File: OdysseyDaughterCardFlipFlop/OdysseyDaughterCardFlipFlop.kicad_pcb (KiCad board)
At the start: 2 copper layers, 39.9 x 46.6 mm, 17 parts, among them J1 Conn_01x02, Q1 2N3906, Q2 2N3906, Q3 BC547C, Q4 BC547C, X1 OdysseyDaughterCard

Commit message: OdysseyDaughterCardFlipFlop: Open and close in Kicad 6, fix symbol library path
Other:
- net class Default removed

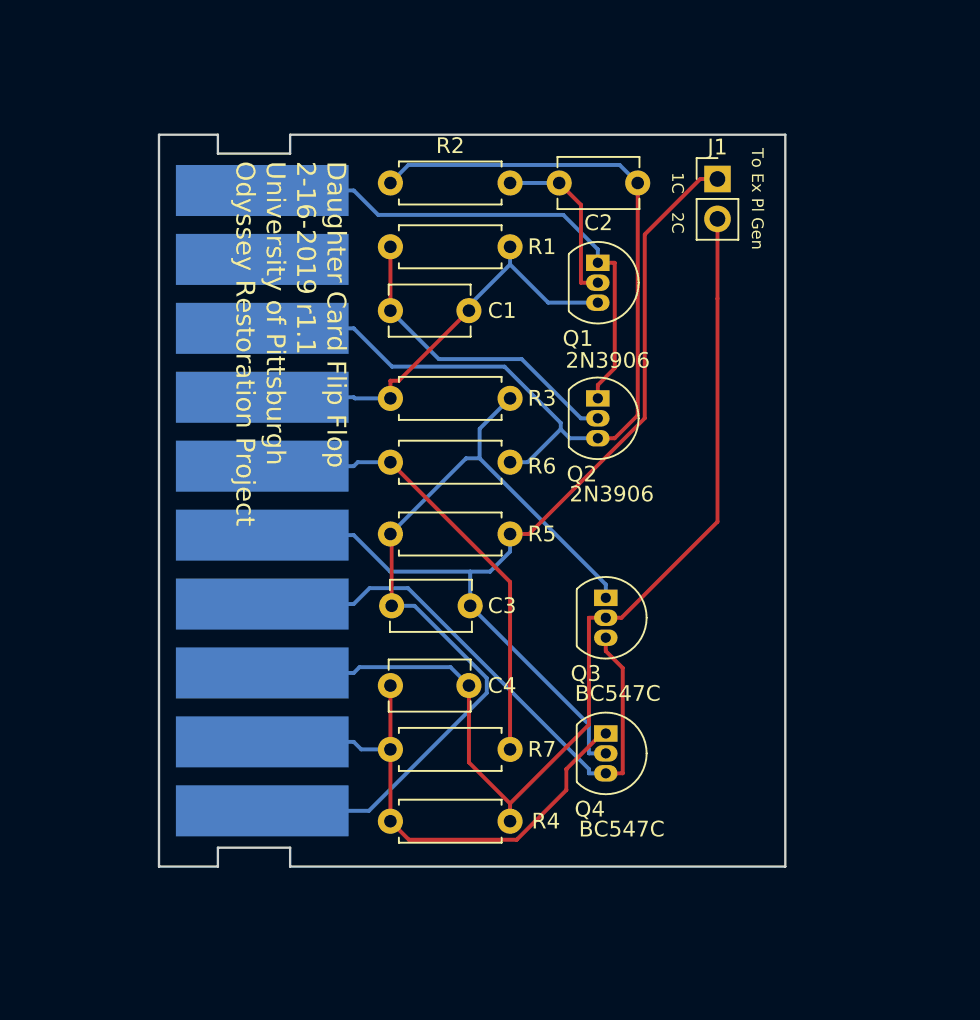
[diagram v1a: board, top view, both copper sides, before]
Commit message: OdysseyDaughterCardFlipFlop wider transistor footprint, logo, pours, pdfs, images, 3d model
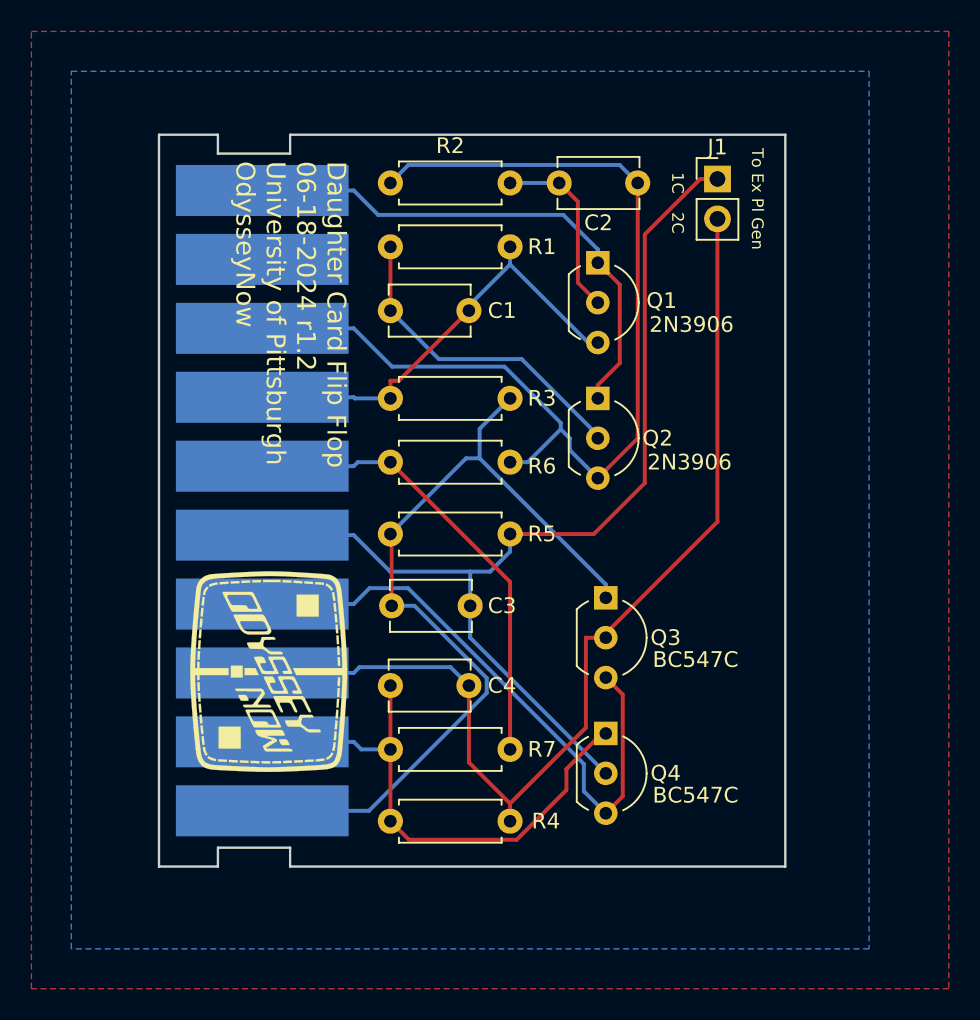
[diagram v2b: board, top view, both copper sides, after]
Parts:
- added X1: OdysseyNow_Logo, Odyssey_Daughter_Card:OdysseyNowLogo, F.Cu at (130.2, 111.6)
- Q1, Q2, Q3, Q4: footprint Package_TO_SOT_THT:TO-92_Inline -> Package_TO_SOT_THT:TO-92_Inline_Wide
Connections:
- X1 pad 9: (no net) -> /Card9
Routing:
- net /Card8: track 63.2 -> 66.6 mm
- net /Card5: track 63.6 -> 66.7 mm
- net GND: track 37.5 -> 38.8 mm
- net /Card7: track 27.9 -> 29.0 mm
- net Net-(Q2-B): track 20.1 -> 20.8 mm
- net Net-(Q1-B): track 11.1 -> 11.8 mm
- net /Card3: track 67.4 -> 66.8 mm
- added copper zone on F.Cu, net /Card10
- added copper zone on B.Cu, net GND
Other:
- board text added: "Daughter Card Flip Flop 06-18-2024 r1.2 University of Pittsburgh OdysseyNow"
- board text removed: "Daughter Card Flip Flop 2-16-2019 r1.1 University of Pittsburgh Odyssey Restoration Project"
